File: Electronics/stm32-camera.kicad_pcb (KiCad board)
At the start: 2 copper layers, 38 x 38.9 mm, 57 parts, among them CON1 MOLEX_47309-2651, P1 HEADER_MALE_2MM_01X06, P2 MOLEX_PICO_PTH_VERT_2_WAY, Q1 VEMT3700, U1 STM32F429VET6, U2 AP2210K-ADJ, U3 AP2210K-ADJ, U4 AP2210K-ADJ, U5 OV02640-VL9A, X1 CSTCE8M00G55Z, X2 SWD

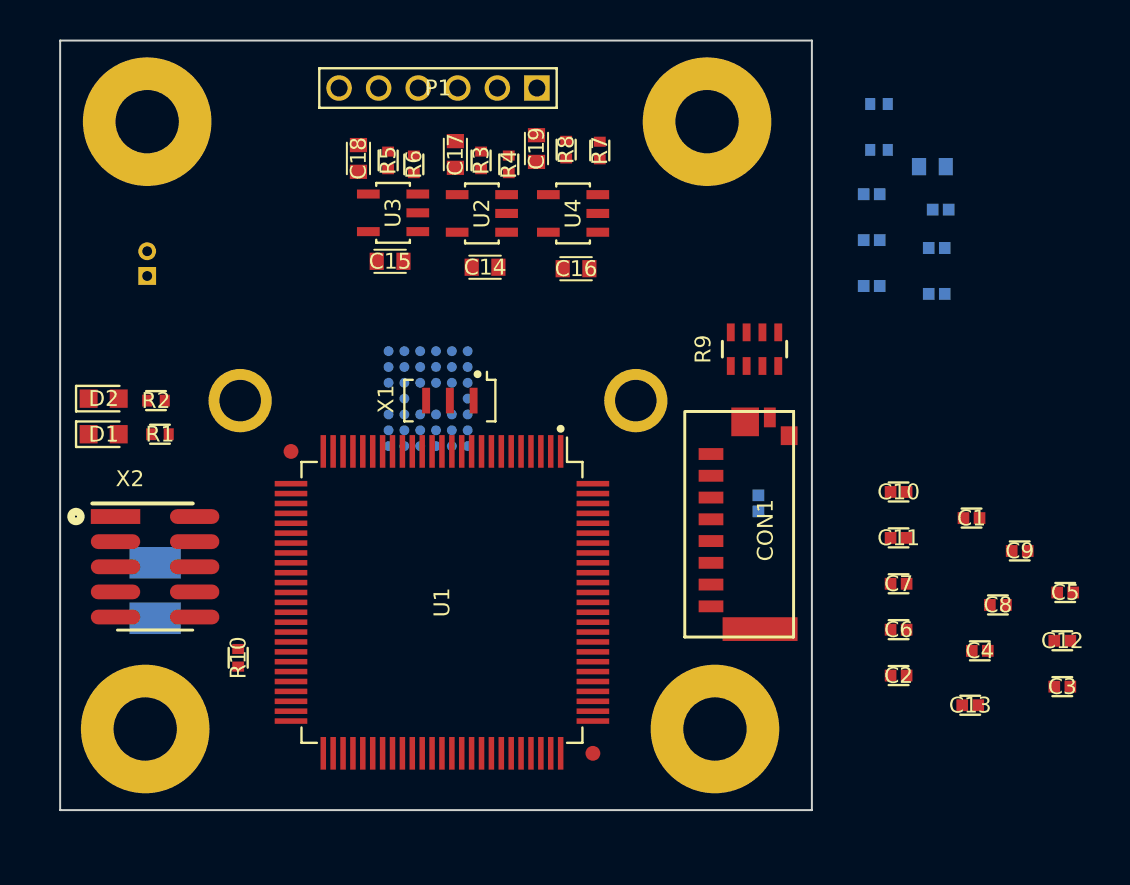
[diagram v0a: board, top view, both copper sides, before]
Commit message: Part layout tests and changed some pin allocations.
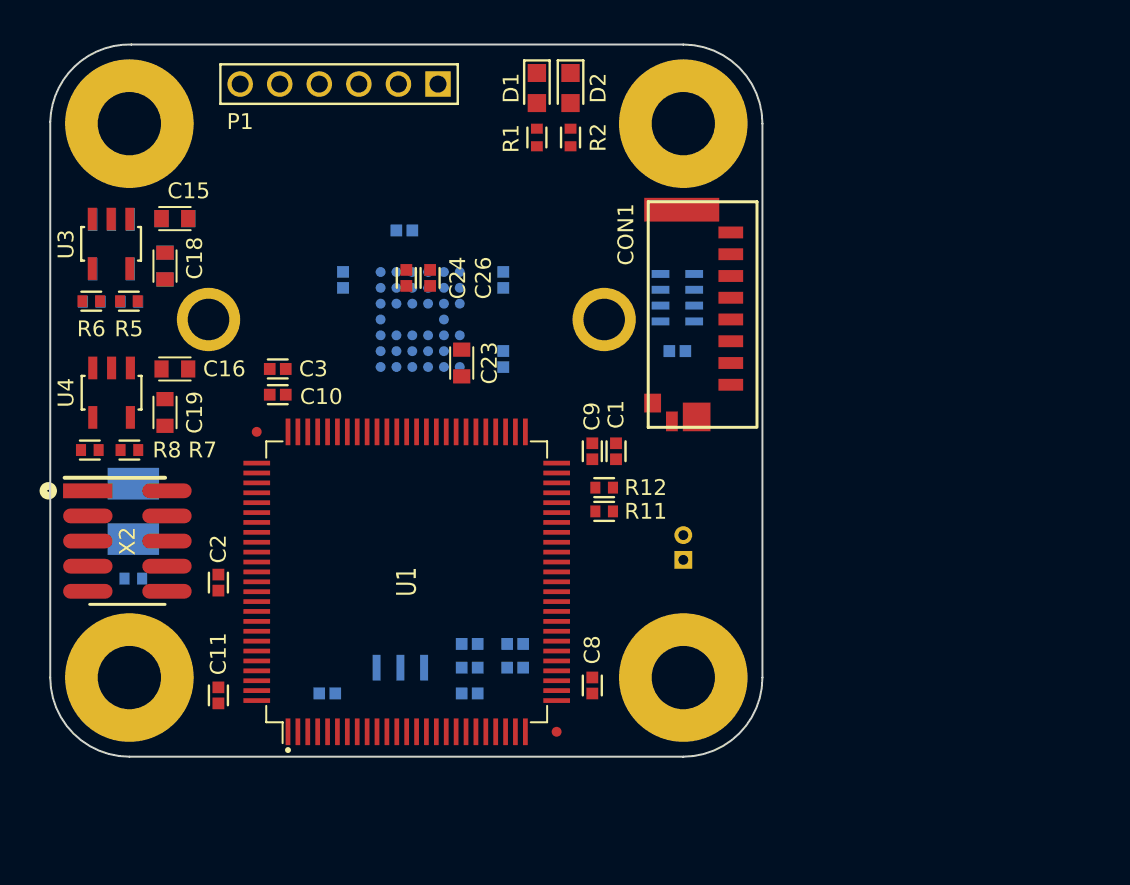
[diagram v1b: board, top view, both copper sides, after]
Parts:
- C12, C13, C14, C17, C4, C5, C6, C7, R10, R3, R4, R9, U2, X1: moved to B.Cu
- C23, C24, C26, R11, R12: moved to F.Cu
- U1: footprint Applidyne_QFP:QFP50P1600X1600X160-100L25N -> Applidyne_QFP:QFP50P1600X1600X160-100L25L
- moved C3 42.8 mm to (111.5, 116.4), turned to 180 degrees
- moved C11 35.3 mm to (108.5, 132.9), turned to 90 degrees
- moved C2 34.7 mm to (108.5, 127.2), turned to 90 degrees
- moved C10 31.8 mm to (111.5, 117.7)
- moved P2 30.7 mm to (132.0, 126.0)
- moved C12 30.0 mm to (121.2, 130.3), turned to 180 degrees
- moved C6 29.1 mm to (114.0, 132.8), turned to 180 degrees
- moved R8 28.5 mm to (102.0, 120.5), turned to 180 degrees
- moved D2 28.3 mm to (126.3, 102.2), turned to 270 degrees
- moved R7 28.2 mm to (104.0, 120.5), turned to 180 degrees
- moved D1 28.0 mm to (124.6, 102.2), turned to 270 degrees
- moved C5 27.9 mm to (123.5, 130.3)
- moved C24 27.2 mm to (118.0, 111.8), turned to 90 degrees
- moved C22 27.1 mm to (114.8, 111.9), turned to 90 degrees
- moved C21 26.9 mm to (117.9, 109.4)
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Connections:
- P1 pad 5: Net-(P1-Pad5) -> (no net)
- P1 pad 6: Net-(P1-Pad6) -> (no net)
- U1 pad 16: Net-(U1-Pad16) -> (no net)
- U1 pad 17: Net-(U1-Pad17) -> (no net)
- U1 pad 18: Net-(U1-Pad18) -> (no net)
- U1 pad 23: Net-(U1-Pad23) -> (no net)
- U1 pad 26: Net-(U1-Pad26) -> (no net)
- U1 pad 30: FLASH_DAC -> (no net)
- U1 pad 32: Net-(U1-Pad32) -> (no net)
- U1 pad 33: Net-(U1-Pad33) -> (no net)
- U1 pad 34: Net-(U1-Pad34) -> (no net)
- U1 pad 35: Net-(U1-Pad35) -> (no net)
- U1 pad 36: Net-(U1-Pad36) -> (no net)
- U1 pad 38: Net-(U1-Pad38) -> IRCUT_A
- U1 pad 39: Net-(U1-Pad39) -> IRCUT_A
- U1 pad 40: Net-(U1-Pad40) -> IRCUT_A
- U1 pad 41: Net-(U1-Pad41) -> IRCUT_A
- U1 pad 42: Net-(U1-Pad42) -> IRCUT_B
- U1 pad 43: Net-(U1-Pad43) -> IRCUT_B
- U1 pad 44: Net-(U1-Pad44) -> IRCUT_B
- U1 pad 45: Net-(U1-Pad45) -> IRCUT_B
- U1 pad 46: Net-(U1-Pad46) -> (no net)
- U1 pad 5: Net-(U1-Pad5) -> (no net)
- U1 pad 51: Net-(U1-Pad51) -> (no net)
- U1 pad 52: Net-(U1-Pad52) -> (no net)
- U1 pad 53: Net-(U1-Pad53) -> (no net)
- U1 pad 54: Net-(U1-Pad54) -> (no net)
- U1 pad 55: IRCUT_A -> (no net)
- U1 pad 56: IRCUT_A -> (no net)
- U1 pad 57: IRCUT_A -> (no net)
- U1 pad 58: IRCUT_A -> (no net)
- U1 pad 59: IRCUT_B -> (no net)
- U1 pad 60: IRCUT_B -> (no net)
- U1 pad 61: IRCUT_B -> (no net)
- U1 pad 62: IRCUT_B -> (no net)
- U1 pad 7: Net-(U1-Pad7) -> (no net)
- U1 pad 71: Net-(U1-Pad71) -> (no net)
- U1 pad 77: Net-(U1-Pad77) -> (no net)
- U1 pad 8: Net-(U1-Pad8) -> (no net)
- U1 pad 82: Net-(U1-Pad82) -> (no net)
- U1 pad 84: Net-(U1-Pad84) -> (no net)
- U1 pad 85: Net-(U1-Pad85) -> (no net)
- U1 pad 86: Net-(U1-Pad86) -> (no net)
- U1 pad 87: Net-(U1-Pad87) -> (no net)
- U1 pad 9: Net-(U1-Pad9) -> (no net)
- U1 pad 94: /Microcontroller/BOOT0 -> (no net)
- U1 pad 95: REBOOT_LATCH -> (no net)
- U5 pad D6: Net-(U5-PadD6) -> (no net)
- U5 pad E1: Net-(U5-PadE1) -> (no net)
- U5 pad E2: Net-(U5-PadE2) -> (no net)
- X2 pad 7: Net-(X2-Pad7) -> (no net)
- X2 pad 8: Net-(X2-Pad8) -> (no net)
- X2 pad 9: Net-(X2-Pad9) -> (no net)
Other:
- board size 38 x 38.9 mm -> 36 x 36 mm
- net class Default: clearance 0.2 -> 0.15; trace_width 0.25 -> 0.16; via_dia 0.8 -> 0.6; via_drill 0.4 -> 0.3
- rule pad_to_mask_clearance: 0 -> 0.1
- rule trace_clearance: 0.2 -> 0.15
- rule trace_min: 0.2 -> 0.16
- rule via_min_size: 0.4 -> 0.45
- board text added: "Board Manufacture Information 1.6mm FR4, 1oz (35um) copper ? Layer ENIG Surface Finish Black Soldermask White Silkscreen Min Track: 0.16mm Min Clearance: 0.16mm Min Via: 0.3mm"

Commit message: Repinned parts of micro to improve routing chances. Part placement, changed footprints etc. Added note in firmware folder to collate thoughts.
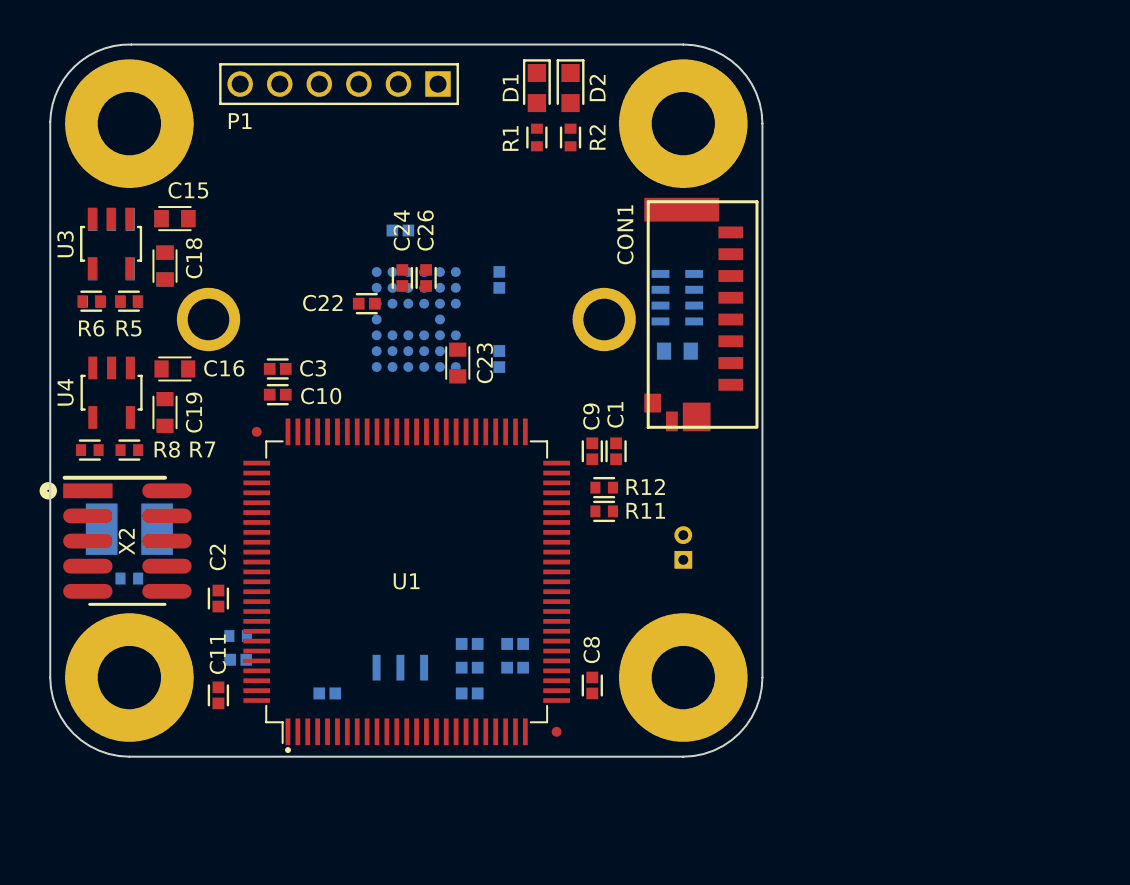
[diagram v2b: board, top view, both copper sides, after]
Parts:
- added C28: 1UF_X5R_1005M, Applidyne_Capacitor:CAPC1005X60N, B.Cu at (109.5, 131.1)
- added R13: 510K_1005M, Applidyne_Resistor:RESC1005X40N, B.Cu at (109.5, 129.9)
- C20: value 1UF_X5R_1005M -> 2.2UF_X7R_1608M; footprint Applidyne_Capacitor:CAPC1005X60N -> Applidyne_Capacitor:CAPC1608X90L
- C22: moved to F.Cu
- X1: value CSTCE8M00G55Z -> CSTCE16M0V53A
- moved C22 1.70 mm to (116.0, 113.1), turned to 180 degrees
- moved Q1 0.92 mm to (104.0, 124.5), turned to 0 degrees
- moved C2 0.80 mm to (108.5, 128.0), turned to 270 degrees
- moved C21 0.20 mm to (117.7, 109.4)
- moved C23 0.20 mm to (120.6, 116.1)
- moved C24 0.20 mm to (117.8, 111.8)
- moved C25 0.20 mm to (122.7, 111.9)
- moved C26 0.20 mm to (119.0, 111.8)
- moved C27 0.20 mm to (122.7, 115.9)
- moved R10 0.20 mm to (104.0, 127.0)
- moved U5 0.20 mm to (118.5, 113.9)
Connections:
- R9 pad 5: MICROSD_D2 -> MICROSD_D1
- R9 pad 6: MICROSD_D3 -> MICROSD_D0
- R9 pad 7: MICROSD_D0 -> MICROSD_D3
- R9 pad 8: MICROSD_D1 -> MICROSD_D2
- U1 pad 1: RESET -> (no net)
- U1 pad 2: PWDN -> (no net)
- U1 pad 24: STATUS0 -> (no net)
- U1 pad 25: STATUS1 -> (no net)
- U1 pad 46: (no net) -> MICROSD_DETECT
- U1 pad 51: (no net) -> STATUS0
- U1 pad 52: (no net) -> STATUS1
- U1 pad 53: (no net) -> STROBE
- U1 pad 54: (no net) -> EXPSTB
- U1 pad 55: (no net) -> FREX
- U1 pad 70: PWR_EN -> RESET
- U1 pad 71: (no net) -> PWDN
- U1 pad 77: (no net) -> PWR_EN
- U1 pad 81: MICROSD_DETECT -> (no net)
- U1 pad 88: STROBE -> (no net)
- U1 pad 90: FREX -> (no net)
- U1 pad 91: EXPSTB -> (no net)
- U1 pad 94: (no net) -> REBOOT_LATCH
- U1 pad 95: (no net) -> REBOOT_LATCH
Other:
- copper layers 2 -> 4

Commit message: Re-added changes from git index corruption issue. Unsure how much recovered.
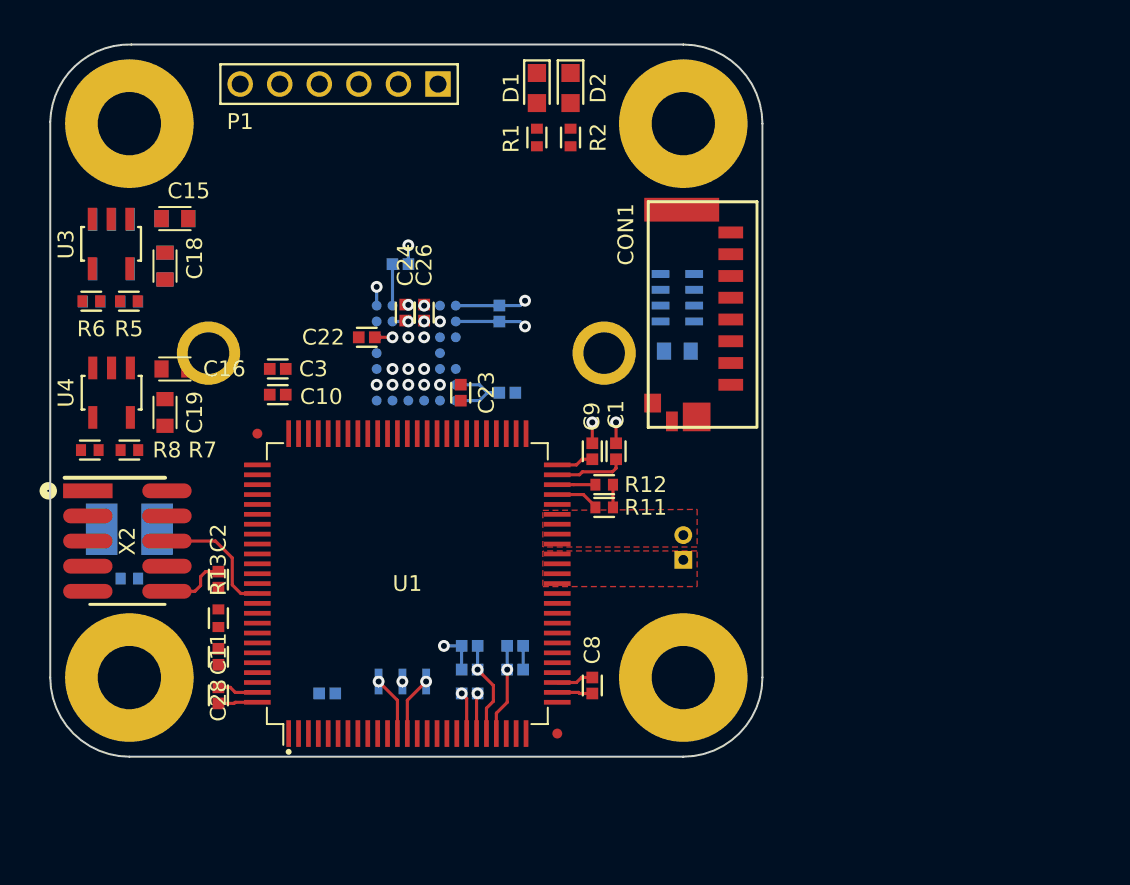
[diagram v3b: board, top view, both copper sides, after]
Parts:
- C23: value 4.7UF_X5R_1608M -> 4.7UF_X5R_1005M; footprint Applidyne_Capacitor:CAPC1608X90L -> Applidyne_Capacitor:CAPC1005X60N
- C28, R13: moved to F.Cu
- moved C24 1.76 mm to (118.0, 113.5)
- moved C26 1.75 mm to (118.9, 113.5)
- moved C27 1.75 mm to (123.1, 117.6), turned to 0 degrees
- moved C22 1.70 mm to (116.0, 114.8)
- moved C21 1.70 mm to (117.7, 111.1)
- moved C25 1.70 mm to (122.7, 113.6)
- moved MP1 1.70 mm to (118.0, 115.6)
- moved U5 1.70 mm to (118.5, 115.6)
- moved C23 1.51 mm to (120.8, 117.6)
- moved R13 1.35 mm to (108.5, 129.0), turned to 90 degrees
- moved C28 1.01 mm to (108.5, 130.9), turned to 270 degrees
- moved C2 0.95 mm to (108.5, 127.0)
- moved X1 0.71 mm to (117.8, 132.2)
- moved R11 0.20 mm to (128.0, 123.4)
- moved R12 0.15 mm to (128.0, 122.2)
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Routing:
- net +3.3V: track 0.00 -> 26.4 mm, vias 0 -> 4
- net GND: track 0.00 -> 15.9 mm, vias 0 -> 10
- net SWO: track 0.00 -> 6.47 mm
- net Net-(C1-Pad1): track 0.00 -> 3.56 mm
- net NRST: track 0.00 -> 3.28 mm
- net Net-(U1-Pad13): track 0.00 -> 3.02 mm, vias 0 -> 1
- net Net-(U1-Pad12): track 0.00 -> 3.02 mm, vias 0 -> 1
- net SIO_C: track 0.00 -> 2.22 mm
- net Net-(C21-Pad1): track 0.00 -> 2.10 mm
- net SIO_D: track 0.00 -> 1.93 mm
- net STROBE: track 0.00 -> 0.95 mm, vias 0 -> 1
- net Net-(C22-Pad1): track 0.00 -> 0.89 mm, vias 0 -> 1
- net +2.8V: track 0.00 -> 0.80 mm, vias 0 -> 2
- net XCLK: vias 0 -> 1
- net PIXCK: vias 0 -> 1
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- added copper zone on In1.Cu, net GND
- added copper zone on F.Cu, net IRCUT_A
- added copper zone on F.Cu, net IRCUT_B

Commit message: Routing concepts
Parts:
- C14, C17, R3, R4, U2: moved to F.Cu
- moved R4 17.3 mm to (119.3, 111.2)
- moved R3 17.3 mm to (121.2, 111.1), turned to 180 degrees
- moved U2 17.3 mm to (120.3, 108.0), turned to 180 degrees
- moved C17 17.2 mm to (122.9, 109.0)
- moved C14 17.1 mm to (123.3, 106.6)
- moved C15 10.5 mm to (116.4, 105.8)
- moved C18 10.5 mm to (115.9, 108.2)
- moved R5 10.5 mm to (114.1, 110.0)
- moved R6 10.5 mm to (112.2, 110.0)
- moved U3 10.5 mm to (113.2, 107.1)
- moved C16 9.06 mm to (109.5, 107.9), turned to 270 degrees
- moved C19 8.84 mm to (109.5, 110.5)
- moved R7 8.84 mm to (107.7, 112.5)
- moved R8 8.84 mm to (105.7, 112.5)
- moved U4 8.84 mm to (106.8, 109.5)
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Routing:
- net VSYNC: track 0.00 -> 23.0 mm, vias 0 -> 1
- net HREF: track 0.00 -> 22.3 mm
- net D4: track 0.00 -> 20.5 mm, vias 1 -> 2
- net D6: track 0.00 -> 19.9 mm, vias 1 -> 2
- net PIXCK: track 0.00 -> 19.7 mm
- net D3: track 0.00 -> 18.0 mm
- net D2: track 0.00 -> 17.3 mm, vias 1 -> 2
- net D7: track 0.00 -> 16.4 mm
- net STATUS0: track 0.00 -> 15.9 mm
- net STATUS1: track 0.00 -> 15.2 mm
- net STROBE: track 0.95 -> 15.4 mm
- net MICROSD_D3: track 0.00 -> 14.0 mm
- net MICROSD_CMD: track 0.00 -> 14.0 mm
- net MICROSD_D2: track 0.00 -> 13.8 mm
- net MICROSD_CK: track 0.00 -> 13.7 mm
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- added copper zone on F.Cu, net +1.3V
- added copper zone on F.Cu, net +2.8V
- added copper zone on F.Cu, net +BATT
- added copper zone on In2.Cu, net GND

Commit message: Update loose pcb files
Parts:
- moved CON1 0.20 mm to (134.4, 113.5)
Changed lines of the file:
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@@
   (general
     (links 185)
-    (no_connects 118)
+    (no_connects 105)
     (area 89.900001 93.54 208.228571 138.767143)
     (thickness 1.6)
@@
     (47 F.CrtYd user hide)
     (48 B.Fab user hide)
-    (49 F.Fab user hide)
+    (49 F.Fab user)
   )
   (setup
@@
   )
   (module Applidyne_Connector_Molex:MOLEX_47309-2651 (layer F.Cu)
-    (at 134.4 113.35 270)
+    (at 134.4 113.55 270)
     (descr http://www.molex.com/pdm_docs/sd/473092651_sd.pdf)
     (tags "SMD SD Card socket compact")
